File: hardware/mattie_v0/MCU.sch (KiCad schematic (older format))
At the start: 9 parts

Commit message: update
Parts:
- added C1, C2, C3, C4, C5, C6: 2.2u, Capacitor_SMD:C_0603_1608Metric, symbol Device:C_Small
- added D1, D2, D3: LED_Small, LED_SMD:LED_0603_1608Metric, symbol Device:LED_Small
- added J1: Conn_02x04_Odd_Even, Connector_PinHeader_1.27mm:PinHeader_2x04_P1.27mm_Vertical, symbol Connector_Generic:Conn_02x04_Odd_Even
- added J2: USB_B_Mini, Connector_USB:USB_Mini-B_Lumberg_2486_01_Horizontal, symbol Connector:USB_B_Mini
- added R1, R2, R3: 1K, Resistor_SMD:R_0603_1608Metric, symbol Device:R_Small
- added R4, R5: 22R, Resistor_SMD:R_0603_1608Metric, symbol Device:R_Small
- gave numbers to parts that had none: 9
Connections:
- net +3V3: now also C1.1, C2.1, C3.1, C4.1, C5.1, C6.1
- net GND: now also C1.2, C2.2, C3.2, C4.2, C5.2, C6.2, D1.1 (K), D2.1 (K), D3.1 (K), J2.5 (GND), J2.6 (Shield)
- net DAT10: now reaches U1.10 (PC2(ADC123_IN12))
- net DAT11: now reaches U1.11 (PC3(ADC123_IN13))
- net DAT0: now reaches U1.14 (PA0(ADC123_IN0/WKUP))
- net DAT1: now reaches U1.15 (PA1(ADC123_IN1))
- net DAT2: now reaches U1.16 (PA2(ADC123_IN2))
- net DAT3: now reaches U1.17 (PA3(ADC123_IN3))
- net GPIO7: now reaches U1.2 (PC13_(RTC_AF1))
- net GPIO7: now also J1.8 (Pin_8)
- net DAT4: now reaches U1.20 (PA4(ADC12_IN4/DAC1_OUT))
- net DAT5: now reaches U1.21 (PA5(ADC12_IN5/DAC2_OUT))
- net DAT6: now reaches U1.22 (PA6(ADC12_IN6))
- net DAT7: now reaches U1.23 (PA7(ADC12_IN7))
- net DAT12: now reaches U1.24 (PC4(ADC12_IN14))
- net DAT13: now reaches U1.25 (PC5(ADC12_IN15))
- net ADC12_IN8: now reaches U1.26 (PB0(ADC12_IN8))
- net ADC12_IN9: now reaches U1.27 (PB1(ADC12_IN9))
- net LED_RED: now reaches U1.29 (PB10)
- net LED_RED: now also R3.1
- net GPIO0: now reaches U1.30 (PB11)
- net GPIO0: now also J1.1 (Pin_1)
- net GPIO1: now reaches U1.33 (PB12)
- net GPIO1: now also J1.2 (Pin_2)
- net GPIO2: now reaches U1.34 (PB13(OTG_HS_VBUS))
- net GPIO2: now also J1.3 (Pin_3)
- net GPIO3: now reaches U1.35 (PB14)
- net GPIO3: now also J1.4 (Pin_4)
- net GPIO4: now reaches U1.36 (PB15)
- net GPIO4: now also J1.5 (Pin_5)
- net DAT14: now reaches U1.37 (PC6)
- net DAT15: now reaches U1.38 (PC7)
- net AUX3: now reaches U1.39 (PC8)
- net AUX4: now reaches U1.40 (PC9)
- net AUX0: now reaches U1.41 (PA8)
- net AUX1: now reaches U1.42 (PA9(OTG_FS_VBUS))
- net AUX2: now reaches U1.43 (PA10)
- net at U1.44 (PA11): now also R4.1
- net at U1.45 (PA12): now also R5.1
- net AUX5: now reaches U1.51 (PC10)
- net GPIO5: now reaches U1.52 (PC11)
- net GPIO5: now also J1.6 (Pin_6)
- net GPIO6: now reaches U1.53 (PC12)
- net GPIO6: now also J1.7 (Pin_7)
- net LED_GREEN: now reaches U1.61 (PB8)
- net LED_GREEN: now also R1.1
- net LED_YELLOW: now reaches U1.62 (PB9)
- net LED_YELLOW: now also R2.1
- net DAT8: now reaches U1.8 (PC0(ADC123_IN10))
- net DAT9: now reaches U1.9 (PC1(ADC123_IN11))
- new net: D1.2 (A), R1.2
- new net: D3.2 (A), R3.2
- new net: D2.2 (A), R2.2
- new net MCU_USB_DM: J2.2 (D-), R4.2
- new net MCU_USB_DP: J2.3 (D+), R5.2
- new net MCU_USB_VBUS: J2.1 (VBUS)
- no-connect marks 4 -> 6
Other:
- note added: "place close to pin 1, 19, 32, 48, 64, 13\n\n"

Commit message: dcdc
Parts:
- J1: value Conn_02x04_Odd_Even -> GPIO
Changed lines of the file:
@@
 P 1800 5550
 F 0 "J1" V 1804 5730 50  0000 L CNN
-F 1 "Conn_02x04_Odd_Even" V 1895 5730 50  0000 L CNN
+F 1 "GPIO" V 1895 5730 50  0000 L CNN
 F 2 "Connector_PinHeader_1.27mm:PinHeader_2x04_P1.27mm_Vertical" H 1800 5550 50  0001 C CNN
 F 3 "~" H 1800 5550 50  0001 C CNN

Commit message: some tweaks
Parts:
- U1: footprint (none) -> Package_QFP:LQFP-64_10x10mm_P0.5mm
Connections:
- net GPIO0: now also U1.34 (PB13(OTG_HS_VBUS)); no longer U1.30 (PB11)
- net GPIO1: now also U1.35 (PB14); no longer U1.33 (PB12)
- net GPIO2: now also U1.36 (PB15); no longer U1.34 (PB13(OTG_HS_VBUS))
- net GPIO3: now also U1.52 (PC11); no longer U1.35 (PB14)
- net GPIO4: now also U1.53 (PC12); no longer U1.36 (PB15)
- net GPIO5: now also U1.2 (PC13_(RTC_AF1)); no longer U1.52 (PC11)
- net GPIO6: now also U1.3 (PC14-OSC32_IN); no longer U1.53 (PC12)
- net GPIO7: now also U1.4 (PC15-OSC32_OUT); no longer U1.2 (PC13_(RTC_AF1))
- net SPI_SS: now reaches U1.50 (PA15(JTDI))
- new net PWRGD1V2: U1.33 (PB12)
- new net REG1V2_ON: U1.30 (PB11)
- no-connect marks 6 -> 3
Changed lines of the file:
@@
 F 0 "U1" H 5850 5987 60  0000 C CNN
 F 1 "STM32F40X_LQFP64" H 5850 5881 60  0000 C CNN
-F 2 "" H 5850 3550 60  0000 C CNN
+F 2 "Package_QFP:LQFP-64_10x10mm_P0.5mm" H 5850 3550 60  0000 C CNN
 F 3 "" H 5850 3550 60  0000 C CNN
 	1    5850 3550
@@
 Wire Wire Line
 	7600 2400 7750 2400
-NoConn ~ 7100 2850
 $Comp
 L power:GND #PWR06
@@
 Text Label 7100 2000 0    50   ~ 0
 BOOT0
-NoConn ~ 7100 1500
-NoConn ~ 7100 1400
 $Comp
 L power:GND #PWR?
@@
 Wire Wire Line
 	3100 3800 3250 3800
-Text Label 4600 3600 2    50   ~ 0
+Text Label 4600 3800 2    50   ~ 0
 GPIO0
-Text Label 4600 3700 2    50   ~ 0
+Text Label 4600 3900 2    50   ~ 0
 GPIO1
-Text Label 4600 3800 2    50   ~ 0
+Text Label 4600 4000 2    50   ~ 0
 GPIO2
-Text Label 4600 3900 2    50   ~ 0
+Text Label 4600 5300 2    50   ~ 0
 GPIO3
-Text Label 4600 4000 2    50   ~ 0
+Text Label 4600 5400 2    50   ~ 0
 GPIO4
-Text Label 4600 5300 2    50   ~ 0
+Text Label 4600 5500 2    50   ~ 0
 GPIO5
-Text Label 4600 5400 2    50   ~ 0
-GPIO6
-Text Label 4600 5500 2    50   ~ 0
-GPIO7
 NoConn ~ 4600 5700
 $Comp
@@
 Text Label 1600 5850 3    50   ~ 0
 GPIO7
+Text HLabel 4600 3600 0    50   Input ~ 0
+REG1V2_ON
+Text HLabel 4600 3700 0    50   Input ~ 0
+PWRGD1V2
+Text Label 7100 1400 0    50   ~ 0
+GPIO6
+Text Label 7100 1500 0    50   ~ 0
+GPIO7
+Text HLabel 7100 2850 2    50   Input ~ 0
+SPI_SS
 $EndSCHEMATC

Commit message: update
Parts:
- added C25: 4.7u, Capacitor_SMD:C_0603_1608Metric, symbol Device:C_Small
- D1: value LED_Small -> GREEN
- D2: value LED_Small -> YELLOW
- D3: value LED_Small -> RED
- GPIO2: renamed from J1; footprint Connector_PinHeader_1.27mm:PinHeader_2x04_P1.27mm_Vertical -> Connector_PinHeader_2.54mm:PinHeader_2x04_P2.54mm_Vertical
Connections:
- net GND: now also C25.2
- net MCU_USB_VBUS: now also C25.1
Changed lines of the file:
@@
 Text Label 9850 5400 2    50   ~ 0
 MCU_USB_DP
-Text HLabel 9850 5600 0    50   Input ~ 0
+Text HLabel 9450 5600 0    50   Input ~ 0
 MCU_USB_VBUS
 $Comp
@@
 P 2450 3300
 F 0 "D1" H 2450 3535 50  0000 C CNN
-F 1 "LED_Small" H 2450 3444 50  0000 C CNN
+F 1 "GREEN" H 2450 3444 50  0000 C CNN
 F 2 "LED_SMD:LED_0603_1608Metric" V 2450 3300 50  0001 C CNN
 F 3 "~" V 2450 3300 50  0001 C CNN
@@
 P 2450 4300
 F 0 "D3" H 2450 4535 50  0000 C CNN
-F 1 "LED_Small" H 2450 4444 50  0000 C CNN
+F 1 "RED" H 2450 4444 50  0000 C CNN
 F 2 "LED_SMD:LED_0603_1608Metric" V 2450 4300 50  0001 C CNN
 F 3 "~" V 2450 4300 50  0001 C CNN
@@
 P 2450 3800
 F 0 "D2" H 2450 4035 50  0000 C CNN
-F 1 "LED_Small" H 2450 3944 50  0000 C CNN
+F 1 "YELLOW" H 2450 3944 50  0000 C CNN
 F 2 "LED_SMD:LED_0603_1608Metric" V 2450 3800 50  0001 C CNN
 F 3 "~" V 2450 3800 50  0001 C CNN
@@
 $EndComp
 $Comp
-L Connector_Generic:Conn_02x04_Odd_Even J1
+L Connector_Generic:Conn_02x04_Odd_Even GPIO2
 U 1 1 5EA17BAA
 P 1800 5550
-F 0 "J1" V 1804 5730 50  0000 L CNN
+F 0 "GPIO2" V 1804 5730 50  0000 L CNN
 F 1 "GPIO" V 1895 5730 50  0000 L CNN
-F 2 "Connector_PinHeader_1.27mm:PinHeader_2x04_P1.27mm_Vertical" H 1800 5550 50  0001 C CNN
+F 2 "Connector_PinHeader_2.54mm:PinHeader_2x04_P2.54mm_Vertical" H 1800 5550 50  0001 C CNN
 F 3 "~" H 1800 5550 50  0001 C CNN
 	1    1800 5550
@@
 Text HLabel 7100 2850 2    50   Input ~ 0
 SPI_SS
+$Comp
+L Device:C_Small C?
+U 1 1 5EA6712A
+P 9600 5800
+AR Path="/5E994520/5EA6712A" Ref="C?"  Part="1"
+AR Path="/5E9881B4/5EA6712A" Ref="C25"  Part="1"
+F 0 "C25" H 9692 5846 50  0000 L CNN
+F 1 "4.7u" H 9692 5755 50  0000 L CNN
+F 2 "Capacitor_SMD:C_0603_1608Metric" H 9600 5800 50  0001 C CNN
+F 3 "~" H 9600 5800 50  0001 C CNN
+F 4 " 346-CM105X5R475M25AT " H 9600 5800 50  0001 C CNN "OrderN"
+	1    9600 5800
+	1    0    0    -1
+$EndComp
+$Comp
+L power:GND #PWR032
+U 1 1 5EA6A257
+P 9600 6000
+F 0 "#PWR032" H 9600 5750 50  0001 C CNN
+F 1 "GND" H 9605 5827 50  0000 C CNN
+F 2 "" H 9600 6000 50  0001 C CNN
+F 3 "" H 9600 6000 50  0001 C CNN
+	1    9600 6000
+	1    0    0    -1
+$EndComp
+Wire Wire Line
+	9600 6000 9600 5900
+Wire Wire Line
+	9850 5600 9600 5600
+Wire Wire Line
+	9600 5600 9600 5700
+Connection ~ 9600 5600
+Wire Wire Line
+	9600 5600 9450 5600
 $EndSCHEMATC

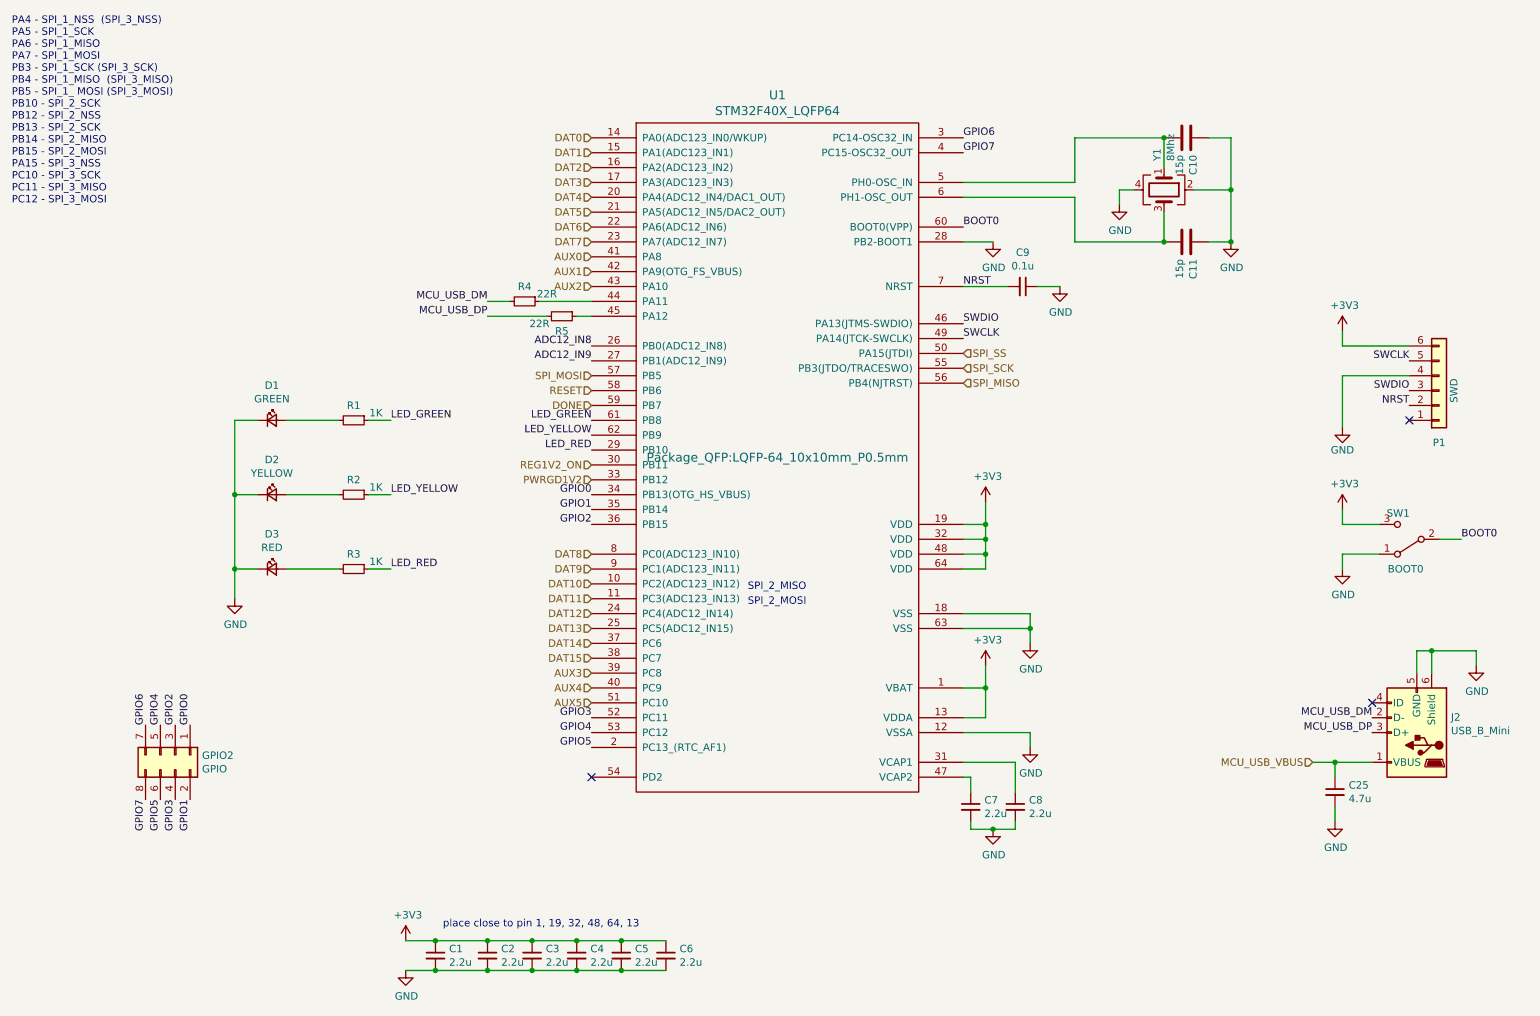
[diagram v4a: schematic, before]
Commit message: added powerswitch for USB power
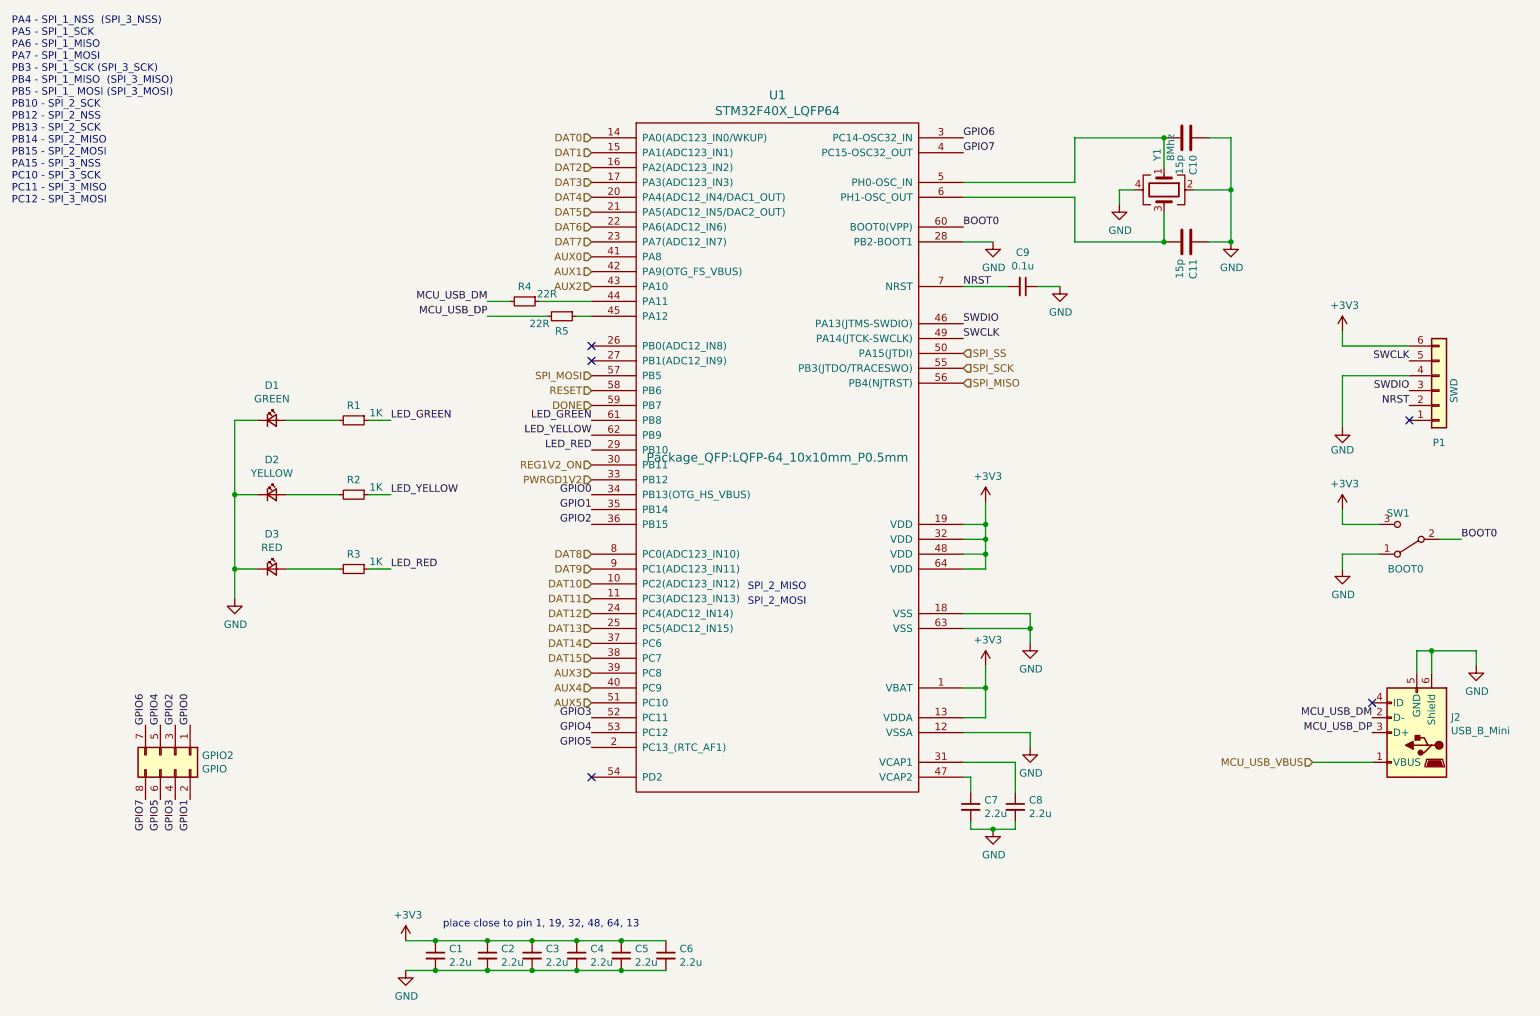
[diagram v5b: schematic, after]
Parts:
- removed C25: 4.7u, Capacitor_SMD:C_0603_1608Metric, symbol Device:C_Small
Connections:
- net ADC12_IN8: no longer names the net of U1.26 (PB0(ADC12_IN8))
- net ADC12_IN9: no longer names the net of U1.27 (PB1(ADC12_IN9))
- no-connect marks 3 -> 5
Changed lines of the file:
@@
 Wire Wire Line
 	8150 1750 8250 1750
-Text Label 4600 2800 2    50   ~ 0
-ADC12_IN8
-Text Label 4600 2900 2    50   ~ 0
-ADC12_IN9
 NoConn ~ 9850 5200
 $Comp
@@
 	1    0    0    -1
 $EndComp
-$Comp
-L Connector:USB_B_Mini J?
-U 1 1 5E9CE687
-P 10150 5400
-AR Path="/5E994520/5E9CE687" Ref="J?"  Part="1"
-AR Path="/5E9881B4/5E9CE687" Ref="J2"  Part="1"
-F 0 "J2" H 9920 5297 50  0000 R CNN
-F 1 "USB_B_Mini" H 9920 5388 50  0000 R CNN
-F 2 "Connector_USB:USB_Mini-B_Lumberg_2486_01_Horizontal" H 10300 5350 50  0001 C CNN
-F 3 "~" H 10300 5350 50  0001 C CNN
-F 4 " 151-1206-1-ND " H 10150 5400 50  0001 C CNN "OrderN"
-	1    10150 5400
-	-1   0    0    1
-$EndComp
 Wire Wire Line
 	10250 5000 10250 4850
@@
 Text Label 9850 5400 2    50   ~ 0
 MCU_USB_DP
-Text HLabel 9450 5600 0    50   Input ~ 0
-MCU_USB_VBUS
 $Comp
 L Device:R_Small R?
@@
 Text HLabel 7100 2850 2    50   Input ~ 0
 SPI_SS
-$Comp
-L Device:C_Small C?
-U 1 1 5EA6712A
-P 9600 5800
-AR Path="/5E994520/5EA6712A" Ref="C?"  Part="1"
-AR Path="/5E9881B4/5EA6712A" Ref="C25"  Part="1"
-F 0 "C25" H 9692 5846 50  0000 L CNN
-F 1 "4.7u" H 9692 5755 50  0000 L CNN
-F 2 "Capacitor_SMD:C_0603_1608Metric" H 9600 5800 50  0001 C CNN
-F 3 "~" H 9600 5800 50  0001 C CNN
-F 4 " 346-CM105X5R475M25AT " H 9600 5800 50  0001 C CNN "OrderN"
-	1    9600 5800
-	1    0    0    -1
-$EndComp
-$Comp
-L power:GND #PWR032
-U 1 1 5EA6A257
-P 9600 6000
-F 0 "#PWR032" H 9600 5750 50  0001 C CNN
-F 1 "GND" H 9605 5827 50  0000 C CNN
-F 2 "" H 9600 6000 50  0001 C CNN
-F 3 "" H 9600 6000 50  0001 C CNN
-	1    9600 6000
-	1    0    0    -1
-$EndComp
-Wire Wire Line
-	9600 6000 9600 5900
-Wire Wire Line
-	9850 5600 9600 5600
-Wire Wire Line
-	9600 5600 9600 5700
-Connection ~ 9600 5600
-Wire Wire Line
-	9600 5600 9450 5600
+Text HLabel 9450 5600 0    50   Input ~ 0
+MCU_USB_VBUS
+$Comp
+L Connector:USB_B_Mini J?
+U 1 1 5E9CE687
+P 10150 5400
+AR Path="/5E994520/5E9CE687" Ref="J?"  Part="1"
+AR Path="/5E9881B4/5E9CE687" Ref="J2"  Part="1"
+F 0 "J2" H 9920 5297 50  0000 R CNN
+F 1 "USB_B_Mini" H 9920 5388 50  0000 R CNN
+F 2 "Connector_USB:USB_Mini-B_Lumberg_2486_01_Horizontal" H 10300 5350 50  0001 C CNN
+F 3 "~" H 10300 5350 50  0001 C CNN
+F 4 " 151-1206-1-ND " H 10150 5400 50  0001 C CNN "OrderN"
+	1    10150 5400
+	-1   0    0    1
+$EndComp
+Wire Wire Line
+	9450 5600 9850 5600
+NoConn ~ 4600 2800
+NoConn ~ 4600 2900
 $EndSCHEMATC

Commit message: tweaks
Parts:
- C9: Mouser 963-TMK107BJ104KA-T -> (none); OrderN (none) -> 963-TMK107BJ104KA-T
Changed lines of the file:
@@
 F 2 "Capacitor_SMD:C_0603_1608Metric" H 7500 2400 50  0001 C CNN
 F 3 "~" H 7500 2400 50  0001 C CNN
-F 4 " 963-TMK107BJ104KA-T " H 7500 2400 50  0001 C CNN "Mouser"
+F 4 "" H 7500 2400 50  0001 C CNN "Mouser"
+F 5 " 963-TMK107BJ104KA-T " H 7500 2400 50  0001 C CNN "OrderN"
 	1    7500 2400
 	0    1    1    0
